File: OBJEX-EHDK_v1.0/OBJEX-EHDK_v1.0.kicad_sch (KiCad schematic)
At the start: 0 parts

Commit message: update sch
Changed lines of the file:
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@@
     )
   )
-  (sheet (at 231.0638 112.0394) (size 41.148 23.876) (fields_autoplaced)
+  (sheet (at 177.6222 100.711) (size 41.148 23.876) (fields_autoplaced)
     (stroke (width 0.1524) (type solid) (color 0 0 0 0))
     (fill (color 0 0 0 0.0000))
-    (property "Sheet name" "ESP32-C3FH4" (id 0) (at 231.0638 111.3278 0)
+    (property "Sheet name" "ESP32-C3FH4" (id 0) (at 177.6222 99.9994 0)
       (effects (font (size 1.27 1.27)) (justify left bottom))
     )
-    (property "Sheet file" "esp32c3fh4.kicad_sch" (id 1) (at 231.0638 136.5 0)
+    (property "Sheet file" "esp32c3fh4.kicad_sch" (id 1) (at 177.6222 125.1716 0)
       (effects (font (size 1.27 1.27)) (justify left top))
     )
@@
       (reference "#PWR?") (unit 1) (value "GND") (footprint "")
     )
+    (path "/0e8b8204-6d33-4185-b260-cc35c8d99e46/0461bfb4-7c00-4a5b-b18a-3d701d3da2dd"
+      (reference "#PWR?") (unit 1) (value "GND") (footprint "")
+    )
     (path "/0e8b8204-6d33-4185-b260-cc35c8d99e46/04b0a2ea-dd14-41ec-90de-e29bf1672385"
       (reference "#PWR?") (unit 1) (value "GND") (footprint "")
@@
       (reference "#PWR?") (unit 1) (value "GND") (footprint "")
     )
+    (path "/0e8b8204-6d33-4185-b260-cc35c8d99e46/6f7da936-dc01-4043-8a36-57cfb7cd7a6e"
+      (reference "#PWR?") (unit 1) (value "GND") (footprint "")
+    )
     (path "/0e8b8204-6d33-4185-b260-cc35c8d99e46/7cc84156-4133-4025-a938-0d4f04421fde"
       (reference "#PWR?") (unit 1) (value "GND") (footprint "")
@@
       (reference "J2") (unit 1) (value "JST_SM02B") (footprint "KicadLibrary:JST_SM02B-SURS-TF(LF)(SN)")
     )
+    (path "/0e8b8204-6d33-4185-b260-cc35c8d99e46/07cef9f4-269c-4729-945f-e2ff23a3d8fd"
+      (reference "J?") (unit 1) (value "Conn_01x05") (footprint "")
+    )
     (path "/c5517dfa-f1e8-47fa-ac1a-f3517e73eb9d/0e8ae8a9-c31f-48ce-8c97-74196f99af3d"
       (reference "J?") (unit 1) (value "Vout1") (footprint "")
@@
       (reference "J?") (unit 1) (value "Bridge BATT_A") (footprint "")
     )
+    (path "/0e8b8204-6d33-4185-b260-cc35c8d99e46/6daf50f3-d51a-4863-971a-d8d875acb299"
+      (reference "J?") (unit 1) (value "Solar") (footprint "")
+    )
     (path "/c5517dfa-f1e8-47fa-ac1a-f3517e73eb9d/7dfc511a-66c1-4aab-9c68-f8e2262796f9"
       (reference "J?") (unit 1) (value "Solar") (footprint "")
     )
-    (path "/c5517dfa-f1e8-47fa-ac1a-f3517e73eb9d/affd4210-f9c1-47a9-8f68-62fa263754e6"
-      (reference "J?") (unit 1) (value "Conn_01x03") (footprint "")
+    (path "/c5517dfa-f1e8-47fa-ac1a-f3517e73eb9d/8dca231a-7a3b-4038-8ee7-0c872c0c7cc9"
+      (reference "J?") (unit 1) (value "Conn_01x02") (footprint "")
+    )
+    (path "/0e8b8204-6d33-4185-b260-cc35c8d99e46/9d5f2eb3-cded-436c-b102-715f44d1bcae"
+      (reference "J?") (unit 1) (value "3V3") (footprint "")
+    )
+    (path "/0e8b8204-6d33-4185-b260-cc35c8d99e46/baa2fef5-84f6-40b6-a0ce-adae4ea6ae51"
+      (reference "J?") (unit 1) (value "1V8") (footprint "")
     )
     (path "/1bd0dc3d-4de3-423e-bb17-63b75cf64400/ce069002-67e1-4069-9d6e-8af6305c11e8"
       (reference "J?") (unit 1) (value "BATT / BACKUP") (footprint "")
     )
+    (path "/c5517dfa-f1e8-47fa-ac1a-f3517e73eb9d/e2b7fa87-df8b-421a-9ffd-70a15db68b2e"
+      (reference "J?") (unit 1) (value "TestPoint - Black") (footprint "")
+    )
     (path "/c5517dfa-f1e8-47fa-ac1a-f3517e73eb9d/ebeb1088-58ce-45a4-b007-277776edb5d8"

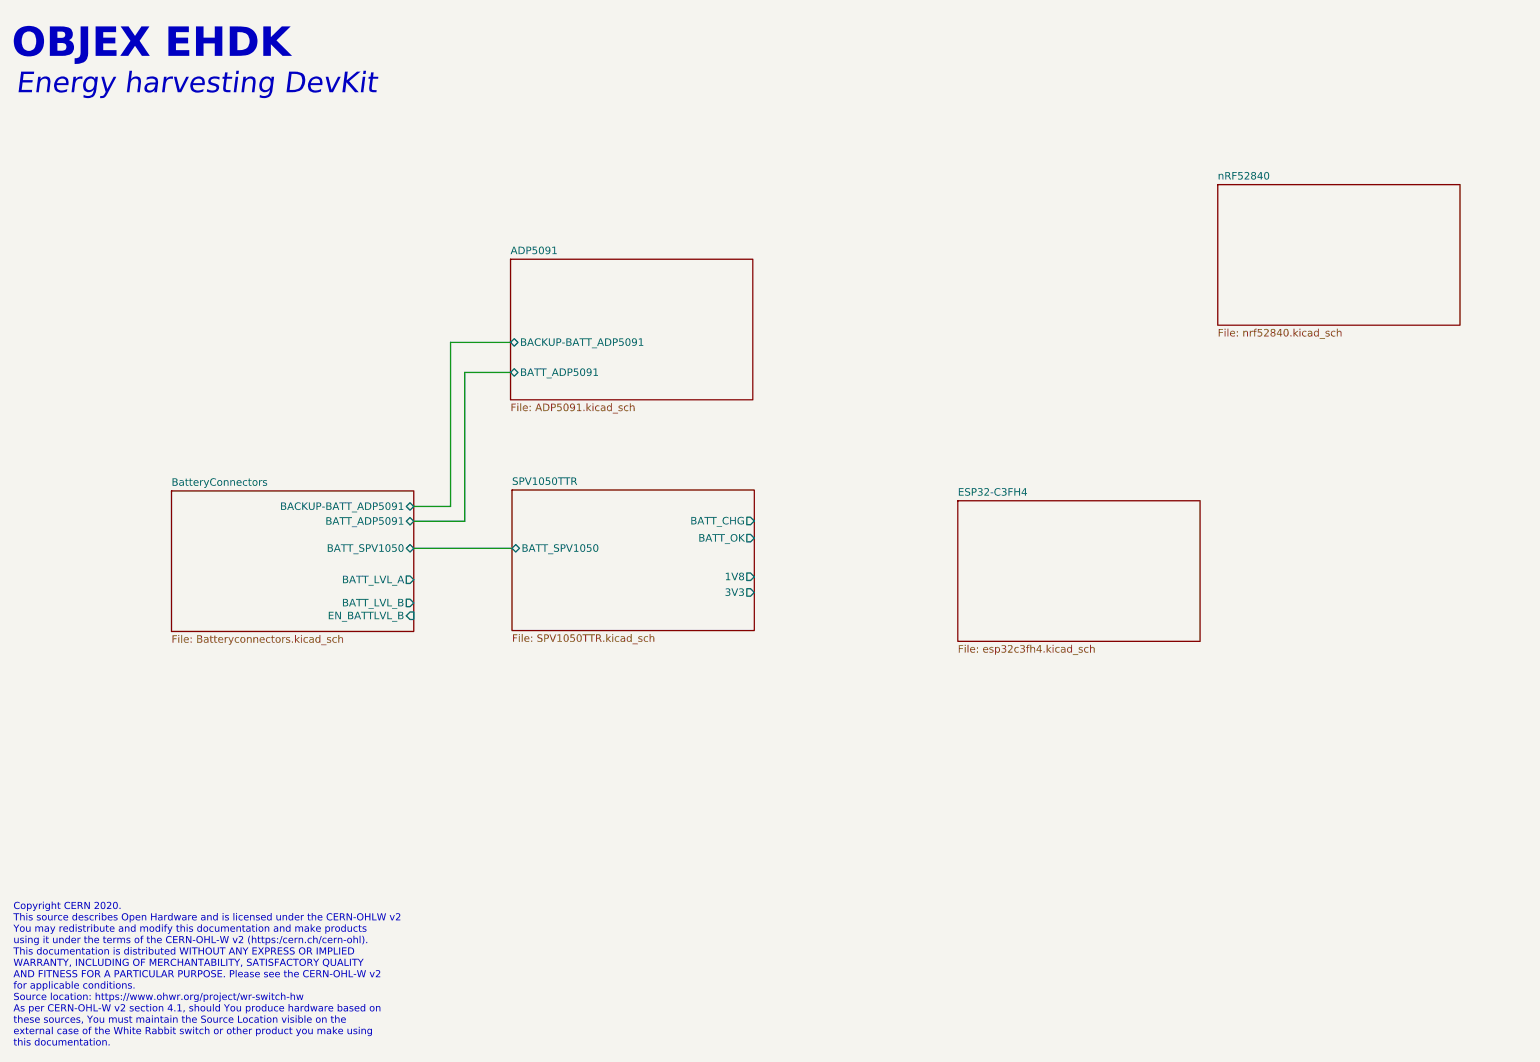
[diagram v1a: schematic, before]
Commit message: Fix, add test points
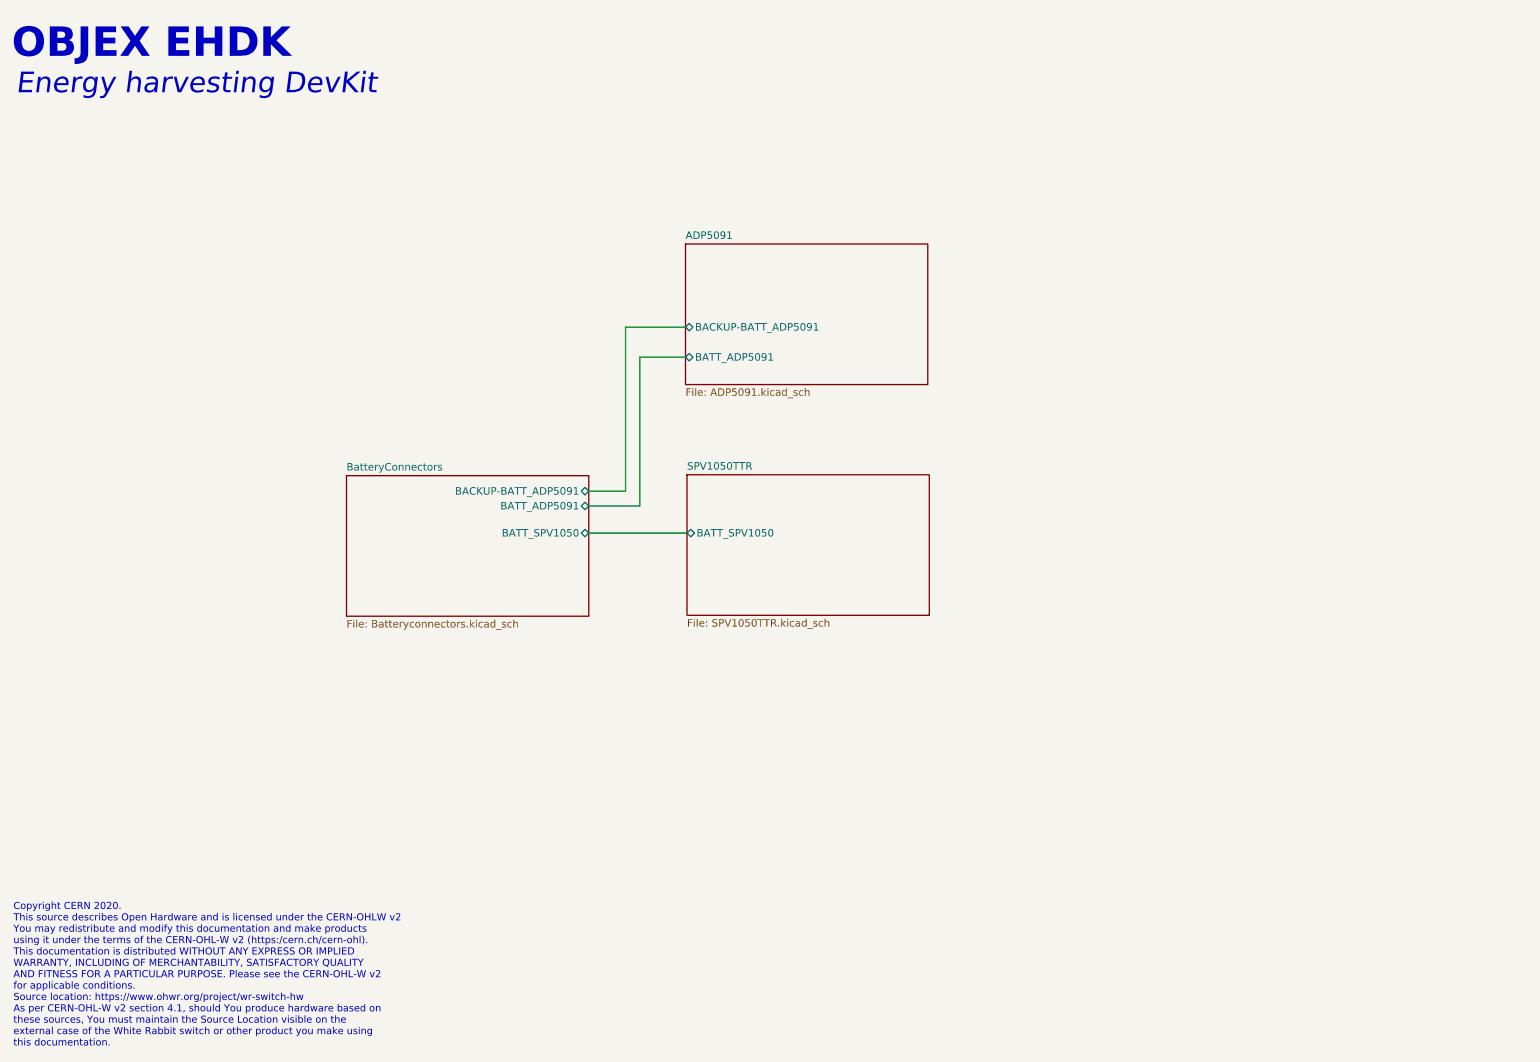
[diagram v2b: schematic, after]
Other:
- removed sheet ESP32-C3FH4
- removed sheet nRF52840
- sheet BatteryConnectors ports: added none; removed BATT_LVL_A, BATT_LVL_B, EN_BATTLVL_B
- sheet SPV1050TTR ports: added none; removed 1V8, 3V3, BATT_CHG, BATT_OK

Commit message: SCH Ready for first review
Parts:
- added H1, H2, H3, H4: M3 - ISO14580, MountingHole:MountingHole_3.2mm_M3_ISO14580_Pad, symbol Mechanical:MountingHole_Pad
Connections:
- new net: H2.1, H4.1
- new net GND: H1.1, H3.1

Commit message: SCH first review
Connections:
- net GND: now also H2.1, H4.1
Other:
- moved on the sheet: H1, H3
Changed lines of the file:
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@@
     (comment 1 "Designer: Salvatore Raccardi")
   )
-  (junction (at 245.3894 96.647) (diameter 0) (color 0 0 0 0)
-  )
-  (junction (at 245.3894 96.6724) (diameter 0) (color 0 0 0 0)
-  )
-  (junction (at 245.3894 87.7824) (diameter 0) (color 0 0 0 0)
+  (junction (at 245.3894 106.9594) (diameter 0) (color 0 0 0 0)
+  )
+  (junction (at 245.4148 89.1032) (diameter 0) (color 0 0 0 0)
   )
   (wire (pts (xy 119.761 99.6696) (xy 126.0094 99.6696))
     (stroke (width 0) (type default) (color 0 0 0 0))
   )
-  (wire (pts (xy 245.3894 96.647) (xy 245.3894 87.7824))
-    (stroke (width 0) (type default) (color 0 0 0 0))
-  )
-  (wire (pts (xy 245.3894 96.6724) (xy 245.3894 98.1202))
-    (stroke (width 0) (type default) (color 0 0 0 0))
-  )
-  (wire (pts (xy 242.062 96.6724) (xy 245.3894 96.6724))
+  (wire (pts (xy 245.4148 89.1032) (xy 248.8438 89.1032))
+    (stroke (width 0) (type default) (color 0 0 0 0))
+  )
+  (wire (pts (xy 242.0874 89.1032) (xy 245.4148 89.1032))
+    (stroke (width 0) (type default) (color 0 0 0 0))
+  )
+  (wire (pts (xy 245.3894 106.9594) (xy 245.3894 108.4072))
+    (stroke (width 0) (type default) (color 0 0 0 0))
+  )
+  (wire (pts (xy 242.062 106.9594) (xy 245.3894 106.9594))
     (stroke (width 0) (type default) (color 0 0 0 0))
   )
@@
     (stroke (width 0) (type default) (color 0 0 0 0))
   )
-  (wire (pts (xy 248.8184 96.6724) (xy 248.8184 94.2848))
-    (stroke (width 0) (type default) (color 0 0 0 0))
-  )
-  (wire (pts (xy 242.062 94.3102) (xy 242.062 96.6724))
+  (wire (pts (xy 248.8184 106.9594) (xy 248.8184 104.5718))
+    (stroke (width 0) (type default) (color 0 0 0 0))
+  )
+  (wire (pts (xy 242.062 104.5972) (xy 242.062 106.9594))
     (stroke (width 0) (type default) (color 0 0 0 0))
   )
@@
     (stroke (width 0) (type default) (color 0 0 0 0))
   )
-  (wire (pts (xy 245.3894 96.6724) (xy 248.8184 96.6724))
-    (stroke (width 0) (type default) (color 0 0 0 0))
-  )
-  (wire (pts (xy 245.3894 87.7824) (xy 242.0874 87.7824))
-    (stroke (width 0) (type default) (color 0 0 0 0))
-  )
-  (wire (pts (xy 248.8438 87.7824) (xy 248.8438 86.7156))
+  (wire (pts (xy 245.3894 106.9594) (xy 248.8184 106.9594))
+    (stroke (width 0) (type default) (color 0 0 0 0))
+  )
+  (wire (pts (xy 248.8438 89.1032) (xy 248.8438 86.7156))
     (stroke (width 0) (type default) (color 0 0 0 0))
   )
@@
     (stroke (width 0) (type default) (color 0 0 0 0))
   )
-  (wire (pts (xy 242.0874 87.7824) (xy 242.0874 86.741))
-    (stroke (width 0) (type default) (color 0 0 0 0))
-  )
-  (wire (pts (xy 245.3894 87.7824) (xy 248.8438 87.7824))
+  (wire (pts (xy 245.4148 89.1032) (xy 245.4148 90.551))
     (stroke (width 0) (type default) (color 0 0 0 0))
   )
   (wire (pts (xy 119.761 106.7816) (xy 136.4488 106.7816))
+    (stroke (width 0) (type default) (color 0 0 0 0))
+  )
+  (wire (pts (xy 242.0874 86.741) (xy 242.0874 89.1032))
     (stroke (width 0) (type default) (color 0 0 0 0))
   )
@@
     (effects (font (size 3.5 3.5) italic) (justify left bottom))
   )
-  (symbol (lib_id "power:GND") (at 245.3894 98.1202 0) (unit 1)
+  (symbol (lib_id "power:GND") (at 245.3894 108.4072 0) (unit 1)
     (in_bom yes) (on_board yes) (fields_autoplaced)
-    (property "Reference" "#PWR0136" (id 0) (at 245.3894 104.4702 0)
-      (effects (font (size 1.27 1.27)) hide)
-    )
-    (property "Value" "GND" (id 1) (at 245.3894 103.4034 0))
-    (property "Footprint" "" (id 2) (at 245.3894 98.1202 0)
-      (effects (font (size 1.27 1.27)) hide)
-    )
-    (property "Datasheet" "" (id 3) (at 245.3894 98.1202 0)
+    (property "Reference" "#PWR0136" (id 0) (at 245.3894 114.7572 0)
+      (effects (font (size 1.27 1.27)) hide)
+    )
+    (property "Value" "GND" (id 1) (at 245.3894 113.6904 0))
+    (property "Footprint" "" (id 2) (at 245.3894 108.4072 0)
+      (effects (font (size 1.27 1.27)) hide)
+    )
+    (property "Datasheet" "" (id 3) (at 245.3894 108.4072 0)
       (effects (font (size 1.27 1.27)) hide)
     )
     (pin "1")
   )
-  (symbol (lib_id "Mechanical:MountingHole_Pad") (at 242.062 91.7702 0) (unit 1)
+  (symbol (lib_id "Mechanical:MountingHole_Pad") (at 242.062 102.0572 0) (unit 1)
     (in_bom yes) (on_board yes)
-    (property "Reference" "H1" (id 0) (at 236.7026 89.535 0)
-      (effects (font (size 1.27 1.27)) (justify left))
-    )
-    (property "Value" "M3 - ISO14580" (id 1) (at 223.647 91.694 0)
-      (effects (font (size 1.27 1.27)) (justify left))
-    )
-    (property "Footprint" "MountingHole:MountingHole_3.2mm_M3_ISO14580_Pad" (id 2) (at 242.062 91.7702 0)
-      (effects (font (size 1.27 1.27)) hide)
-    )
-    (property "Datasheet" "~" (id 3) (at 242.062 91.7702 0)
+    (property "Reference" "H1" (id 0) (at 236.7026 99.822 0)
+      (effects (font (size 1.27 1.27)) (justify left))
+    )
+    (property "Value" "M3 - ISO14580" (id 1) (at 223.647 101.981 0)
+      (effects (font (size 1.27 1.27)) (justify left))
+    )
+    (property "Footprint" "MountingHole:MountingHole_3.2mm_M3_ISO14580_Pad" (id 2) (at 242.062 102.0572 0)
+      (effects (font (size 1.27 1.27)) hide)
+    )
+    (property "Datasheet" "~" (id 3) (at 242.062 102.0572 0)
       (effects (font (size 1.27 1.27)) hide)
     )
@@
     (pin "1")
   )
-  (symbol (lib_id "Mechanical:MountingHole_Pad") (at 248.8184 91.7448 0) (unit 1)
+  (symbol (lib_id "Mechanical:MountingHole_Pad") (at 248.8184 102.0318 0) (unit 1)
     (in_bom yes) (on_board yes) (fields_autoplaced)
-    (property "Reference" "H3" (id 0) (at 251.8664 89.2047 0)
-      (effects (font (size 1.27 1.27)) (justify left))
-    )
-    (property "Value" "M3 - ISO14580" (id 1) (at 251.8664 91.7447 0)
-      (effects (font (size 1.27 1.27)) (justify left))
-    )
-    (property "Footprint" "MountingHole:MountingHole_3.2mm_M3_ISO14580_Pad" (id 2) (at 248.8184 91.7448 0)
-      (effects (font (size 1.27 1.27)) hide)
-    )
-    (property "Datasheet" "~" (id 3) (at 248.8184 91.7448 0)
+    (property "Reference" "H3" (id 0) (at 251.8664 99.4917 0)
+      (effects (font (size 1.27 1.27)) (justify left))
+    )
+    (property "Value" "M3 - ISO14580" (id 1) (at 251.8664 102.0317 0)
+      (effects (font (size 1.27 1.27)) (justify left))
+    )
+    (property "Footprint" "MountingHole:MountingHole_3.2mm_M3_ISO14580_Pad" (id 2) (at 248.8184 102.0318 0)
+      (effects (font (size 1.27 1.27)) hide)
+    )
+    (property "Datasheet" "~" (id 3) (at 248.8184 102.0318 0)
       (effects (font (size 1.27 1.27)) hide)
     )
@@
     )
     (property "Datasheet" "~" (id 3) (at 248.8438 84.1756 0)
+      (effects (font (size 1.27 1.27)) hide)
+    )
+    (pin "1")
+  )
+  (symbol (lib_id "power:GND") (at 245.4148 90.551 0) (unit 1)
+    (in_bom yes) (on_board yes) (fields_autoplaced)
+    (property "Reference" "#PWR0138" (id 0) (at 245.4148 96.901 0)
+      (effects (font (size 1.27 1.27)) hide)
+    )
+    (property "Value" "GND" (id 1) (at 245.4148 95.8342 0))
+    (property "Footprint" "" (id 2) (at 245.4148 90.551 0)
+      (effects (font (size 1.27 1.27)) hide)
+    )
+    (property "Datasheet" "" (id 3) (at 245.4148 90.551 0)
       (effects (font (size 1.27 1.27)) hide)
     )
@@
       (reference "#PWR0137") (unit 1) (value "GND") (footprint "")
     )
+    (path "/e0fe93aa-01b7-4df1-8aae-5662e8118bb7"
+      (reference "#PWR0138") (unit 1) (value "GND") (footprint "")
+    )
     (path "/1bd0dc3d-4de3-423e-bb17-63b75cf64400/709ea27c-ada8-4cd1-83ef-6adacf2c94d1"

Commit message: last review
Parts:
- added J27: TestPoint - Purple, TestPoint:TestPoint_Loop_D3.80mm_Drill2.0mm, symbol Connector_Generic:Conn_01x01
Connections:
- net GND: now also J27.1 (Pin_1)
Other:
- note added: "Dim foro min 1mm"
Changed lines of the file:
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@@
+    (stroke (width 0) (type default) (color 0 0 0 0))
+  )
+  (wire (pts (xy 236.1946 135.3058) (xy 243.9162 135.3058))
     (stroke (width 0) (type default) (color 0 0 0 0))
   )
@@
     )
   )
+  (text "Dim foro min 1mm" (at 247.3198 140.6398 0)
+    (effects (font (size 1.27 1.27)) (justify left bottom))
+  )
   (text "OBJEX EHDK" (at 16.9418 26.0096 0)
     (effects (font (size 5 5) (thickness 0.8) bold) (justify left bottom))
@@
     (effects (font (size 3.5 3.5) italic) (justify left bottom))
   )
+  (symbol (lib_id "power:GND") (at 236.1946 135.3058 270) (unit 1)
+    (in_bom yes) (on_board yes) (fields_autoplaced)
+    (property "Reference" "#PWR0139" (id 0) (at 229.8446 135.3058 0)
+      (effects (font (size 1.27 1.27)) hide)
+    )
+    (property "Value" "GND" (id 1) (at 232.41 135.3057 90)
+      (effects (font (size 1.27 1.27)) (justify right))
+    )
+    (property "Footprint" "" (id 2) (at 236.1946 135.3058 0)
+      (effects (font (size 1.27 1.27)) hide)
+    )
+    (property "Datasheet" "" (id 3) (at 236.1946 135.3058 0)
+      (effects (font (size 1.27 1.27)) hide)
+    )
+    (pin "1")
+  )
   (symbol (lib_id "power:GND") (at 245.3894 108.4072 0) (unit 1)
     (in_bom yes) (on_board yes) (fields_autoplaced)
@@
     )
     (property "Datasheet" "~" (id 3) (at 242.0874 84.201 0)
+      (effects (font (size 1.27 1.27)) hide)
+    )
+    (pin "1")
+  )
+  (symbol (lib_id "Connector_Generic:Conn_01x01") (at 248.9962 135.3058 0) (unit 1)
+    (in_bom yes) (on_board yes) (fields_autoplaced)
+    (property "Reference" "J27" (id 0) (at 252.1458 134.0357 0)
+      (effects (font (size 1.27 1.27)) (justify left))
+    )
+    (property "Value" "TestPoint - Purple" (id 1) (at 252.1458 136.5757 0)
+      (effects (font (size 1.27 1.27)) (justify left))
+    )
+    (property "Footprint" "TestPoint:TestPoint_Loop_D3.80mm_Drill2.0mm" (id 2) (at 248.9962 135.3058 0)
+      (effects (font (size 1.27 1.27)) hide)
+    )
+    (property "Datasheet" "~" (id 3) (at 248.9962 135.3058 0)
       (effects (font (size 1.27 1.27)) hide)
     )
@@
       (reference "#PWR0138") (unit 1) (value "GND") (footprint "")
     )
+    (path "/0d188ab7-d4c3-4d38-b0af-5fd5226aa8c5"
+      (reference "#PWR0139") (unit 1) (value "GND") (footprint "")
+    )
     (path "/1bd0dc3d-4de3-423e-bb17-63b75cf64400/709ea27c-ada8-4cd1-83ef-6adacf2c94d1"
       (reference "BT1") (unit 1) (value "BAT-HLD-001-TR") (footprint "lib:BAT_BAT-HLD-001-TR")
@@
       (reference "J26") (unit 1) (value "Conn_01x02") (footprint "Connector_PinHeader_2.54mm:PinHeader_1x02_P2.54mm_Vertical")
     )
+    (path "/2fd9fba8-c77f-4f02-83e3-2f19f822695e"
+      (reference "J27") (unit 1) (value "TestPoint - Purple") (footprint "TestPoint:TestPoint_Loop_D3.80mm_Drill2.0mm")
+    )
     (path "/c5517dfa-f1e8-47fa-ac1a-f3517e73eb9d/e1833d7e-e5a2-438d-b465-87d447e8f0e8"
